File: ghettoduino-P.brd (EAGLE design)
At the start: 50 x 38.6 mm, 26 parts

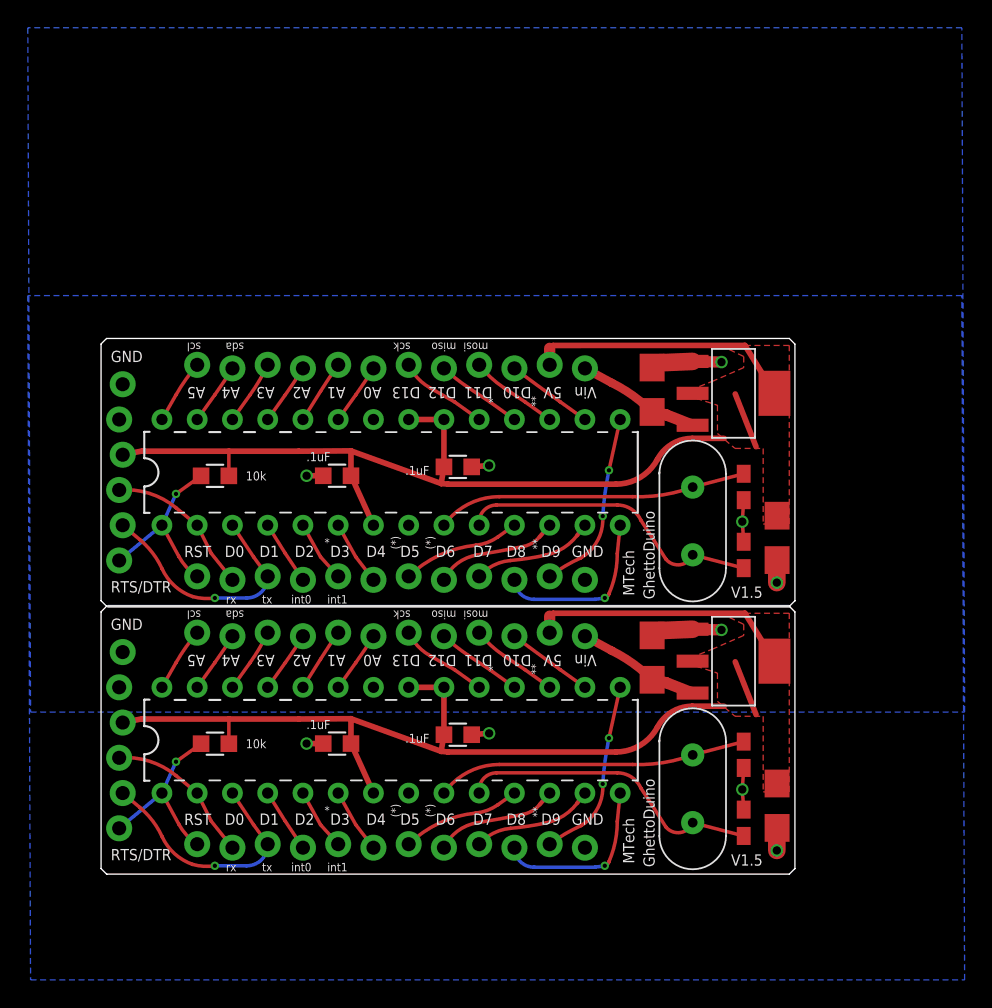
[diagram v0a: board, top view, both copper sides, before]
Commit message: Panelized with new design.
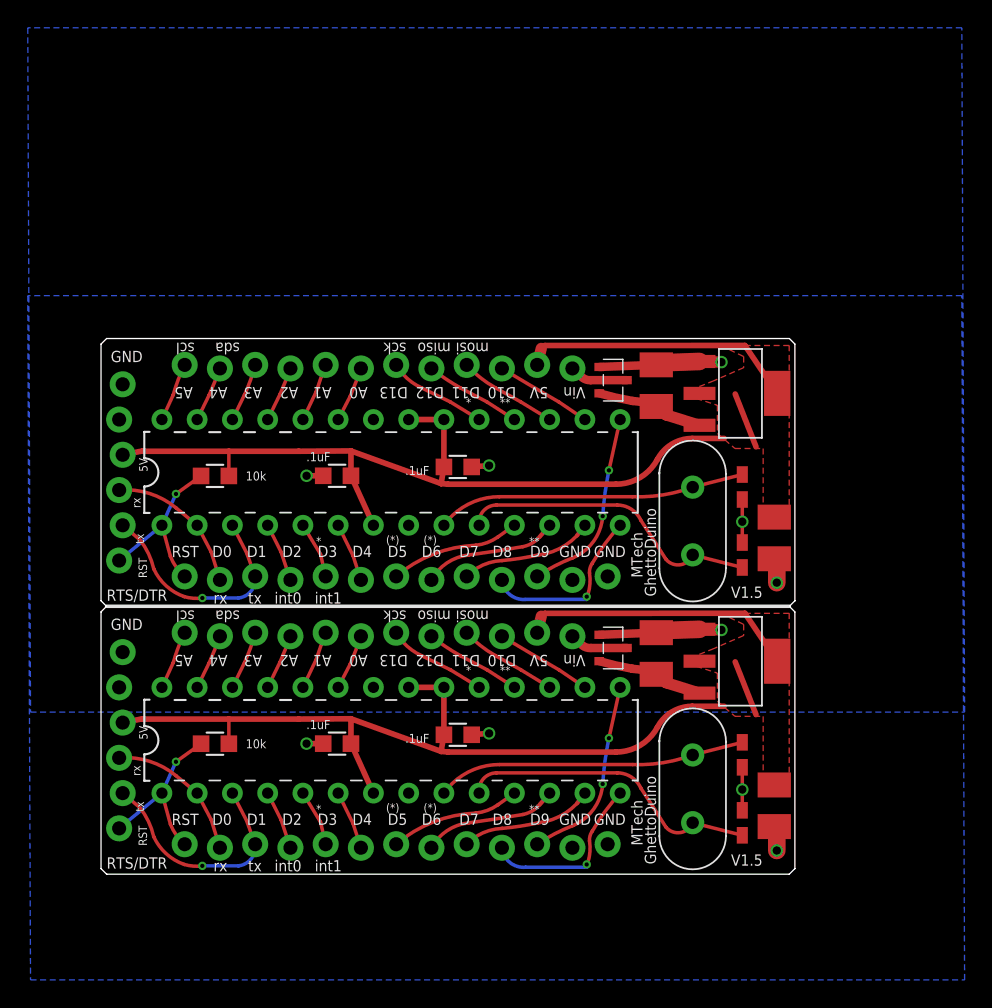
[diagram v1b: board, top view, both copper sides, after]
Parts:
- added U$7: M12, 1dah:1X12_LOCK
- added U$8: P-MOSFET-PMV48XP, 1dah:SOT23-3LEAD
- 5V, 5V1: value ZLDO1117 -> 5V-LDO-ZLDO1117
- U$2, U$6: device 1dah:1X12_LOCK -> 1dah:1X13_LOCK
- U$3: value HC49US -> P-MOSFET-PMV48XP; device 1dah:HC49US -> 1dah:SOT23-3LEAD
- U$4: value M12 -> HC49US; device 1dah:1X12_LOCK -> 1dah:HC49US
- moved U$4 35.9 mm to (42.6, 25.4), turned to 270 degrees
- moved U$6 15.3 mm to (6.03, 21.3)
- moved U$3 10.8 mm to (36.9, 16.3), turned to 90 degrees
- moved U$2 0.90 mm to (6.03, 2.03)
- moved U$5 0.90 mm to (6.03, 17.3)
- moved 5V 0.50 mm to (46.1, 15.3)
- moved 5V1 0.50 mm to (46.1, 34.6)
- moved C12 0.42 mm to (40.0, 35.2)
- moved C8 0.42 mm to (40.0, 15.9)
- moved C11 0.20 mm to (48.5, 24.2)
- moved C5 0.20 mm to (48.5, 4.93)
- moved C6 0.10 mm to (46.2, 23.0)
- moved C3 0.10 mm to (46.2, 3.70)
- moved C1 0.10 mm to (46.2, 8.60)
- moved C7 0.10 mm to (46.2, 27.9)
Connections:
- new net N$1: U$3.3, U$5.12
- new net N$2: U$7.12, U$8.3
- net 5V1: now also U$7.11; no longer U$6.11
- net A10: now also U$7.5; no longer U$6.5
- net A11: now also U$7.6; no longer U$6.6
- net A6: now also U$7.1; no longer U$6.1
- net A7: now also U$7.2; no longer U$6.2
- net A8: now also U$7.3; no longer U$6.3
- net A9: now also U$7.4; no longer U$6.4
- net D14: now also U$6.4; no longer U$4.4
- net D15: now also U$6.5; no longer U$4.5
- net D16: now also U$6.6; no longer U$4.6
- net D17: now also U$6.7; no longer U$4.7
- net D18: now also U$6.8; no longer U$4.8
- net D19: now also U$6.9; no longer U$4.9
- net D20: now also U$6.10; no longer U$4.10
- net D21: now also U$6.11; no longer U$4.11
- net D22: now also U$7.10; no longer U$6.10
- net D23: now also U$7.9; no longer U$6.9
- net D24: now also U$7.8; no longer U$6.8
- net D25: now also U$7.7; no longer U$6.7
- net D26: now also U$6.2; no longer U$4.2
- net D27: now also U$6.3; no longer U$4.3
- net GND: now also U$2.13, U$3.1
- net GND1: now also U$6.12, U$6.13, U$8.1; no longer U$4.12
- net RESET1: now also U$6.1; no longer U$4.1
- net VIN: now also U$3.2; no longer U$5.12
- net VIN1: now also U$8.2; no longer U$6.12
- net XTAL_N1: now also U$4.2; no longer U$3.2
- net XTAL_P1: now also U$4.1; no longer U$3.1
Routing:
- net N$2: track 0.00 -> 4.19 mm
- net N$1: track 0.00 -> 4.19 mm
- net GND1: track 12.2 -> 16.2 mm
- net GND: track 12.2 -> 16.2 mm
- net VIN1: track 8.86 -> 7.67 mm
- net VIN: track 8.86 -> 7.67 mm
- net D1: track 17.8 -> 16.8 mm
- net D27: track 17.8 -> 16.8 mm
- net D18: track 8.85 -> 9.68 mm
- net D6: track 8.85 -> 9.68 mm
- net D17: track 8.49 -> 9.32 mm
- net D5: track 8.49 -> 9.32 mm
- net D19: track 8.70 -> 9.49 mm
- net D7: track 8.70 -> 9.49 mm
- net D24: track 6.28 -> 7.03 mm
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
